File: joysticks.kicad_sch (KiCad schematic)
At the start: 27 parts, among them J1 DB9_Male_MountingHoles, J2 DB9_Male_MountingHoles, J25 Joystick Ports Mezannine Lower, J26 Joystick Ports Mezannine Upper, SW1 Reset Button, U10 74LS06N, U11 74LS06N, U5 74LS06N, U6 74LVC374, U7 74LVC374, U8 74LS374, U9 74LS373

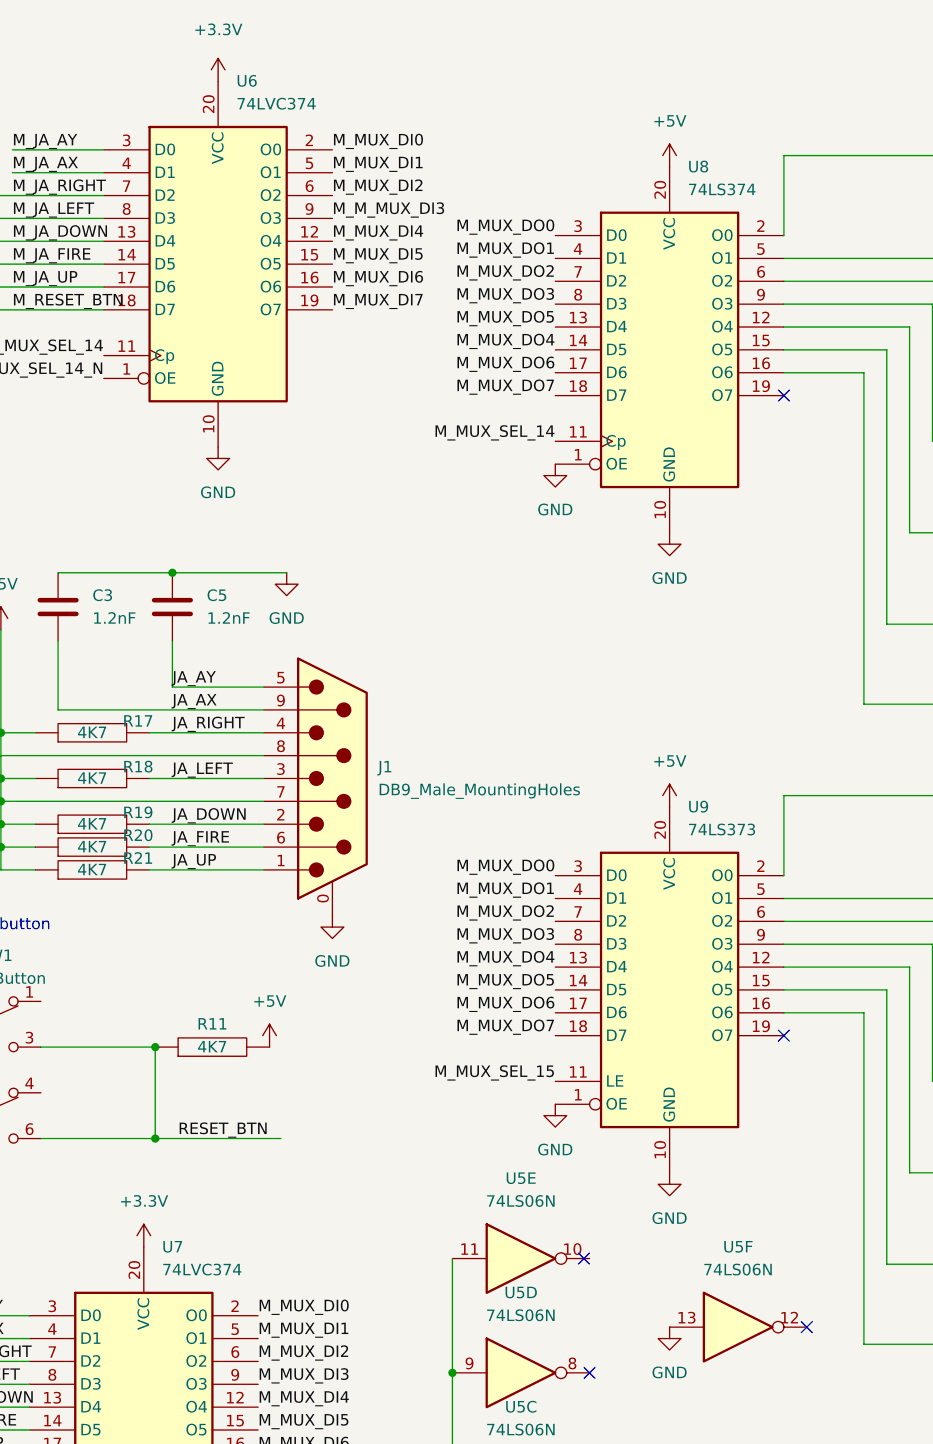
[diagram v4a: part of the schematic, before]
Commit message: add footprints to differentiate 3.3V from 5V ICs
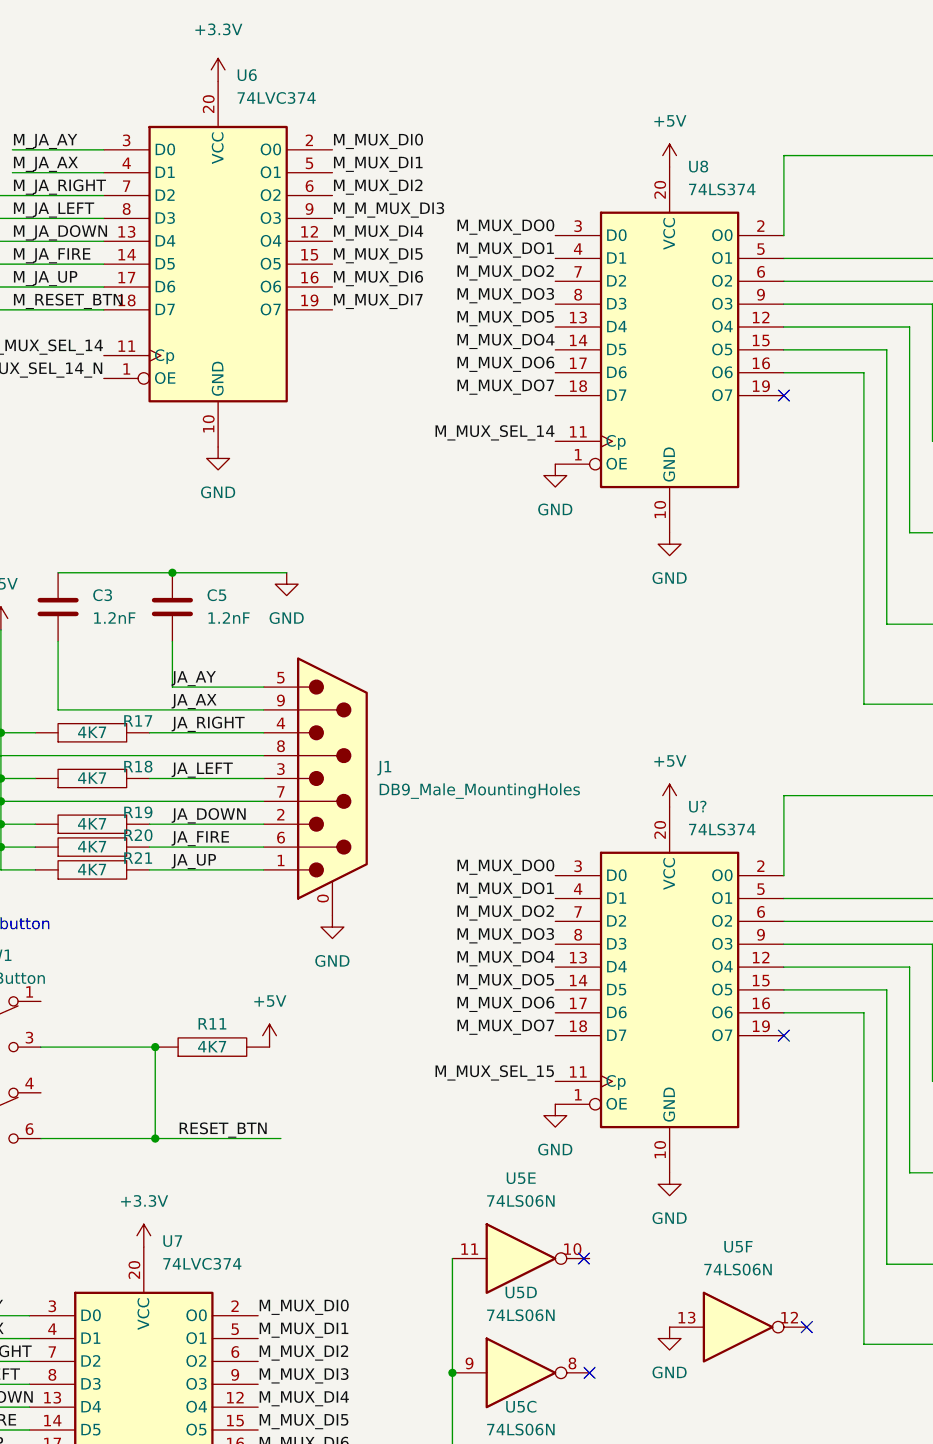
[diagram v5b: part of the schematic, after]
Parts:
- removed U9: 74LS373, Package_DIP:DIP-20_W7.62mm, symbol 74xx:74LS373
- added U?: 74LS374, snapeda:DIP-20_LS_Family, symbol 74xx:74LS374
- U6, U7: footprint Package_DIP:DIP-20_W7.62mm -> snapeda:DIP-20_LVC_Family
- U8: footprint Package_DIP:DIP-20_W7.62mm -> snapeda:DIP-20_LS_Family
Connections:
- net +5V: now also U?.20 (VCC)
- net GND: now also U?.1 (OE), U?.10 (GND)
- net M_MUX_DO0: now also U?.3 (D0)
- net M_MUX_DO1: now also U?.4 (D1)
- net M_MUX_DO2: now also U?.7 (D2)
- net M_MUX_DO3: now also U?.8 (D3)
- net M_MUX_DO4: now also U?.13 (D4)
- net M_MUX_DO5: now also U?.14 (D5)
- net M_MUX_DO6: now also U?.17 (D6)
- net M_MUX_DO7: now also U?.18 (D7)
- net M_MUX_SEL_15: now also U?.11 (Cp)
- net at U10.3: now also U?.5 (O1)
- net at U11.11: now also U?.12 (O4)
- net at U11.13: now also U?.15 (O5)
- net at U11.3: now also U?.16 (O6)
- net at U11.1: now also U?.2 (O0)
- net at U11.5: now also U?.6 (O2)
- net at U11.9: now also U?.9 (O3)
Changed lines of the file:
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@@
   (symbol (lib_id "74xx:74HC374") (at 125.73 169.545 0) (unit 1)
     (in_bom yes) (on_board yes) (fields_autoplaced)
-    (property "Reference" "U7" (id 0) (at 127.7494 149.225 0)
-      (effects (font (size 1.27 1.27)) (justify left))
-    )
-    (property "Value" "74LVC374" (id 1) (at 127.7494 151.765 0)
-      (effects (font (size 1.27 1.27)) (justify left))
-    )
-    (property "Footprint" "Package_DIP:DIP-20_W7.62mm" (id 2) (at 125.73 169.545 0)
+    (property "Reference" "U7" (id 0) (at 127.7494 148.59 0)
+      (effects (font (size 1.27 1.27)) (justify left))
+    )
+    (property "Value" "74LVC374" (id 1) (at 127.7494 151.13 0)
+      (effects (font (size 1.27 1.27)) (justify left))
+    )
+    (property "Footprint" "snapeda:DIP-20_LVC_Family" (id 2) (at 125.73 169.545 0)
       (effects (font (size 1.27 1.27)) hide)
     )
@@
     (pin "2")
   )
-  (symbol (lib_id "74xx:74LS373") (at 184.15 120.65 0) (unit 1)
-    (in_bom yes) (on_board yes) (fields_autoplaced)
-    (property "Reference" "U9" (id 0) (at 186.1694 100.33 0)
-      (effects (font (size 1.27 1.27)) (justify left))
-    )
-    (property "Value" "74LS373" (id 1) (at 186.1694 102.87 0)
-      (effects (font (size 1.27 1.27)) (justify left))
-    )
-    (property "Footprint" "Package_DIP:DIP-20_W7.62mm" (id 2) (at 184.15 120.65 0)
-      (effects (font (size 1.27 1.27)) hide)
-    )
-    (property "Datasheet" "http://www.ti.com/lit/gpn/sn74LS373" (id 3) (at 184.15 120.65 0)
-      (effects (font (size 1.27 1.27)) hide)
-    )
-    (pin "1")
-    (pin "10")
-    (pin "11")
-    (pin "12")
-    (pin "13")
-    (pin "14")
-    (pin "15")
-    (pin "16")
-    (pin "17")
-    (pin "18")
-    (pin "19")
-    (pin "2")
-    (pin "20")
-    (pin "3")
-    (pin "4")
-    (pin "5")
-    (pin "6")
-    (pin "7")
-    (pin "8")
-    (pin "9")
-  )
   (symbol (lib_id "power:+5V") (at 252.095 41.91 90) (unit 1)
     (in_bom yes) (on_board yes) (fields_autoplaced)
@@
   (symbol (lib_id "74xx:74HC374") (at 133.985 40.005 0) (unit 1)
     (in_bom yes) (on_board yes) (fields_autoplaced)
-    (property "Reference" "U6" (id 0) (at 136.0044 19.685 0)
-      (effects (font (size 1.27 1.27)) (justify left))
-    )
-    (property "Value" "74LVC374" (id 1) (at 136.0044 22.225 0)
-      (effects (font (size 1.27 1.27)) (justify left))
-    )
-    (property "Footprint" "Package_DIP:DIP-20_W7.62mm" (id 2) (at 133.985 40.005 0)
+    (property "Reference" "U6" (id 0) (at 136.0044 19.05 0)
+      (effects (font (size 1.27 1.27)) (justify left))
+    )
+    (property "Value" "74LVC374" (id 1) (at 136.0044 21.59 0)
+      (effects (font (size 1.27 1.27)) (justify left))
+    )
+    (property "Footprint" "snapeda:DIP-20_LVC_Family" (id 2) (at 133.985 40.005 0)
       (effects (font (size 1.27 1.27)) hide)
     )
@@
       (effects (font (size 1.27 1.27)) (justify left))
     )
-    (property "Footprint" "Package_DIP:DIP-20_W7.62mm" (id 2) (at 184.15 49.53 0)
+    (property "Footprint" "snapeda:DIP-20_LS_Family" (id 2) (at 184.15 49.53 0)
       (effects (font (size 1.27 1.27)) hide)
     )
@@
     (pin "3")
     (pin "4")
+    (pin "5")
+    (pin "6")
+    (pin "7")
+    (pin "8")
+    (pin "9")
+  )
+  (symbol (lib_id "74xx:74LS374") (at 184.15 120.65 0) (unit 1)
+    (in_bom yes) (on_board yes) (fields_autoplaced)
+    (property "Reference" "U?" (id 0) (at 186.1694 100.33 0)
+      (effects (font (size 1.27 1.27)) (justify left))
+    )
+    (property "Value" "74LS374" (id 1) (at 186.1694 102.87 0)
+      (effects (font (size 1.27 1.27)) (justify left))
+    )
+    (property "Footprint" "snapeda:DIP-20_LS_Family" (id 2) (at 184.15 120.65 0)
+      (effects (font (size 1.27 1.27)) hide)
+    )
+    (property "Datasheet" "http://www.ti.com/lit/gpn/sn74LS374" (id 3) (at 184.15 120.65 0)
+      (effects (font (size 1.27 1.27)) hide)
+    )
+    (pin "1")
+    (pin "10")
+    (pin "11")
+    (pin "12")
+    (pin "13")
+    (pin "14")
+    (pin "15")
+    (pin "16")
+    (pin "17")
+    (pin "18")
+    (pin "19")
+    (pin "2")
+    (pin "20")
+    (pin "3")
+    (pin "4")

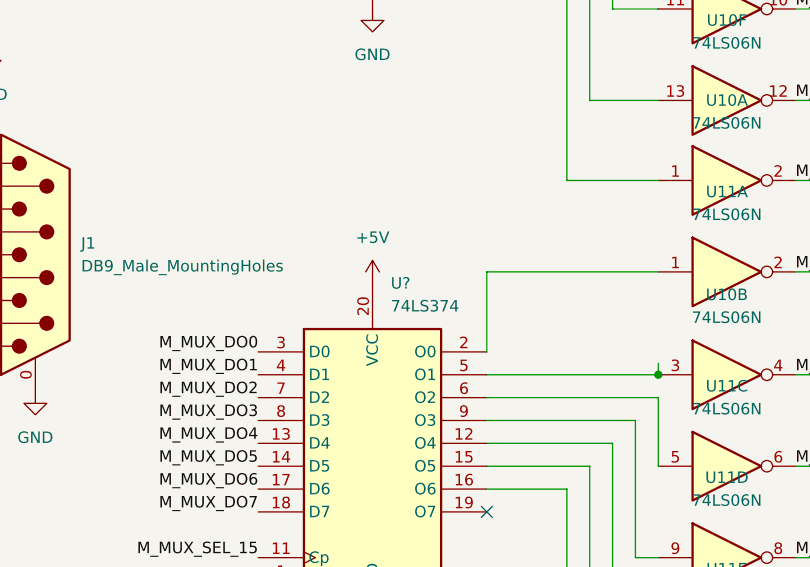
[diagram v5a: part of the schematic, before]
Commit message: try to fix B.silk, add VIN to +12V_FUSED jumper
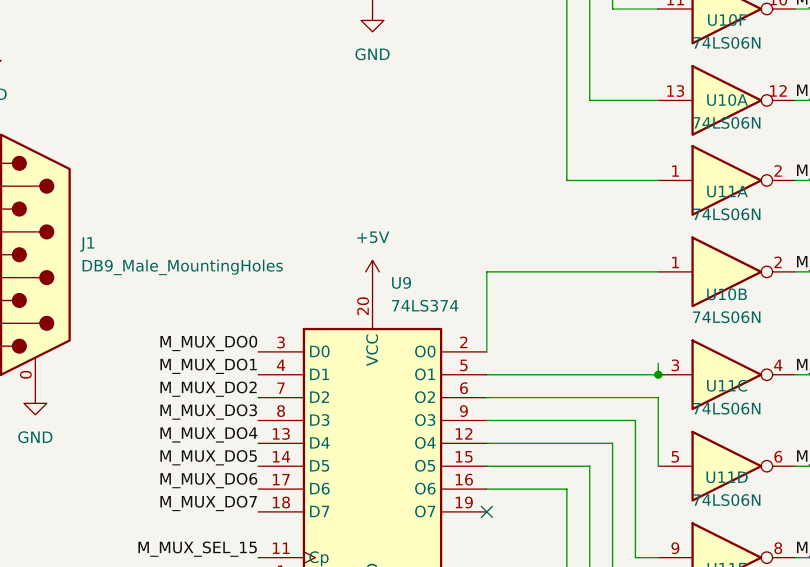
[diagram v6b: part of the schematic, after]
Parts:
- gave numbers to parts that had none: 1
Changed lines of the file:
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@@
   (symbol (lib_id "74xx:74LS374") (at 184.15 120.65 0) (unit 1)
     (in_bom yes) (on_board yes) (fields_autoplaced)
-    (property "Reference" "U?" (id 0) (at 186.1694 100.33 0)
+    (property "Reference" "U9" (id 0) (at 186.1694 100.33 0)
       (effects (font (size 1.27 1.27)) (justify left))
     )

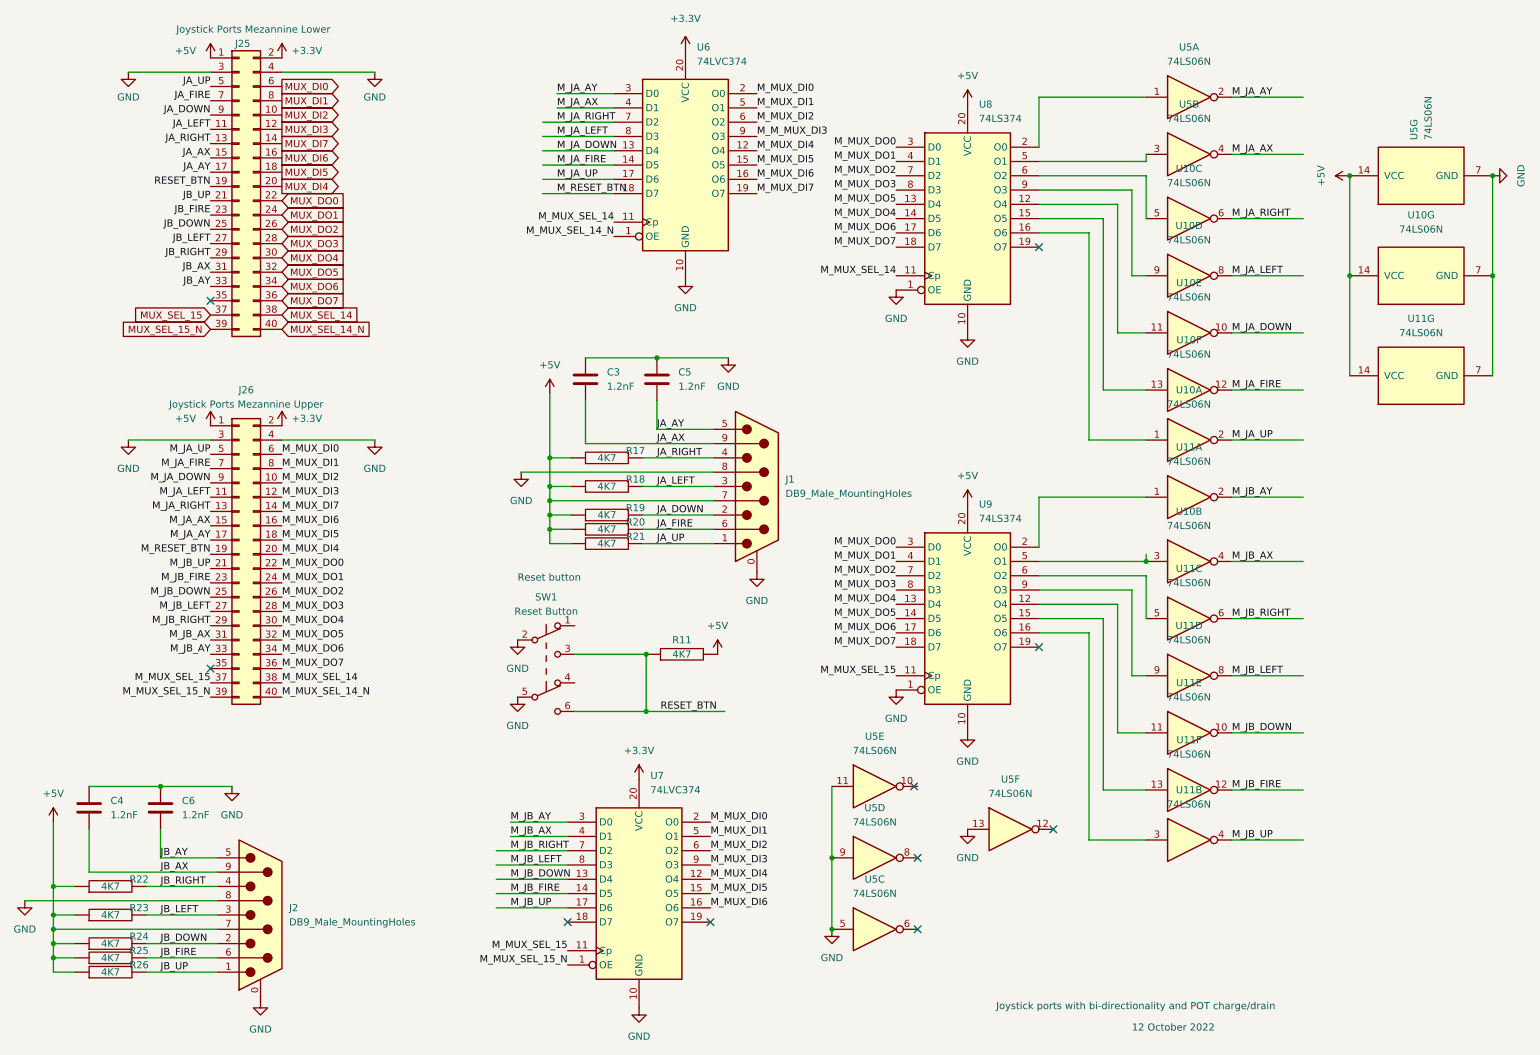
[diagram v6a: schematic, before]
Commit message: fix design rule violations
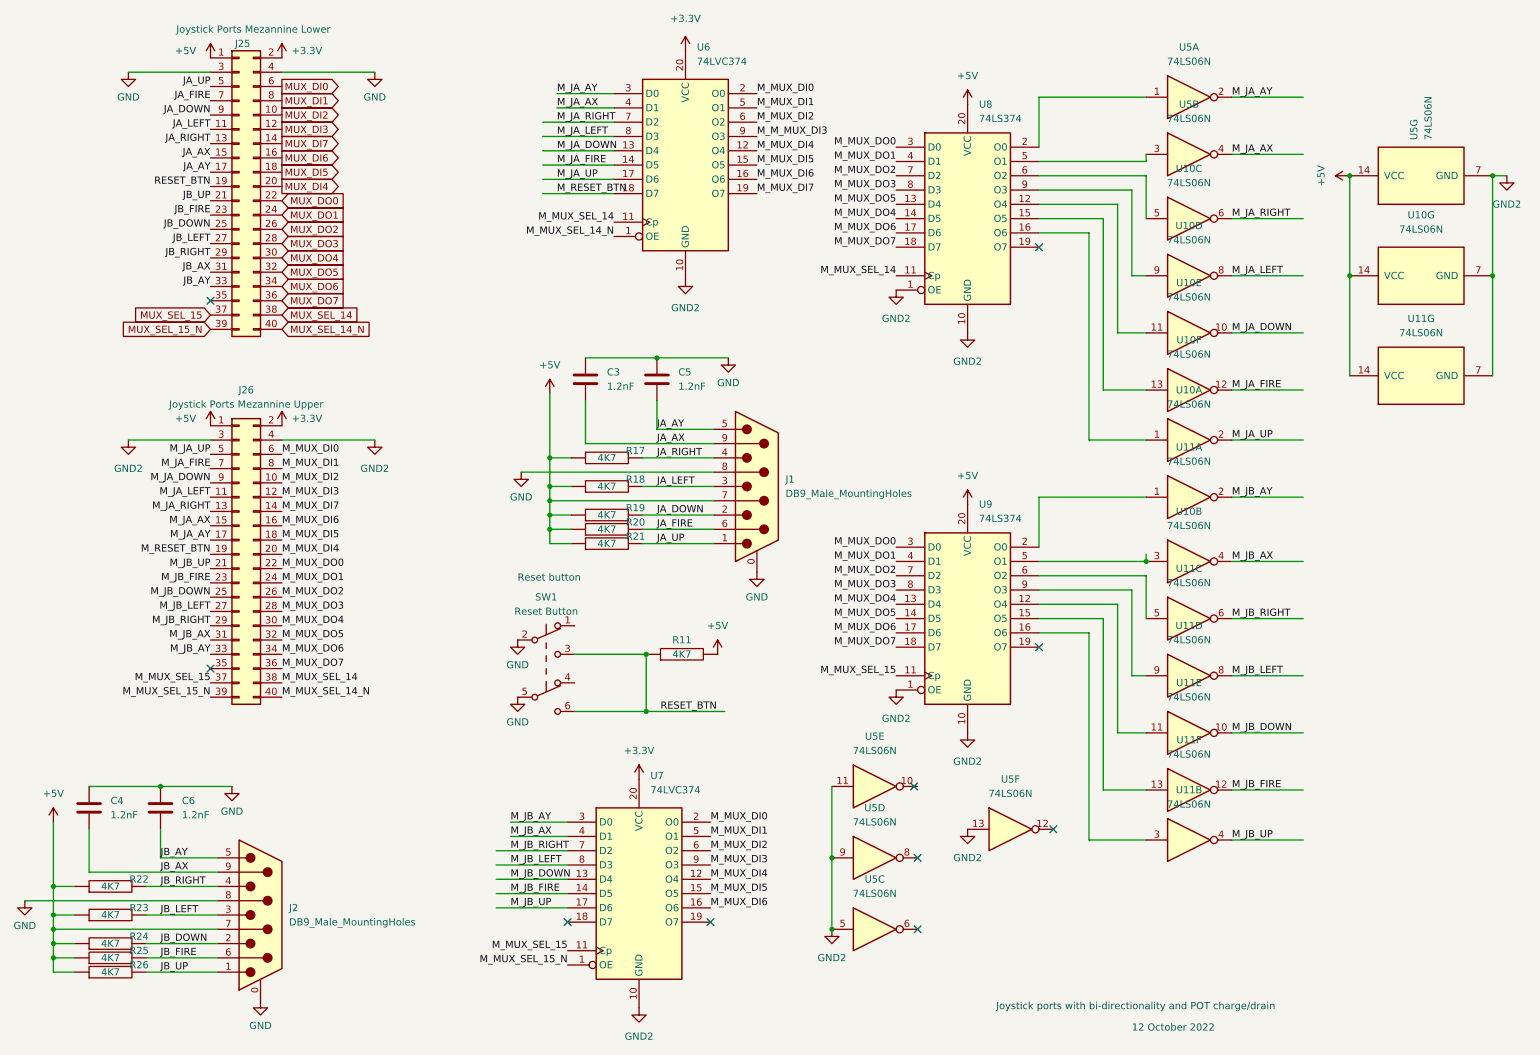
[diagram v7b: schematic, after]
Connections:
- net GND: no longer J26.3 (Pin_3), J26.4 (Pin_4), U10.7 (GND), U11.7 (GND), U5.11, U5.13, U5.5, U5.7 (GND), U5.9, U6.10 (GND), U7.10 (GND), U8.1 (OE), U8.10 (GND), U9.1 (OE), U9.10 (GND)
- new net GND2: J26.3 (Pin_3), J26.4 (Pin_4), U10.7 (GND), U11.7 (GND), U5.11, U5.13, U5.5, U5.7 (GND), U5.9, U6.10 (GND), U7.10 (GND), U8.1 (OE), U8.10 (GND), U9.1 (OE), U9.10 (GND)
